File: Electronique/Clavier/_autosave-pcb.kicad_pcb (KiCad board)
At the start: 2 copper layers, 170 parts, among them J3 Conn_01x05, Q3 BSS84, Q4 BSS138, SW1 A, SW10 R, SW11 F, SW12 C, SW13 T, SW14 G, SW15 V, SW16 Y, SW17 H, SW18 B, SW19 1, SW2 Q, SW20 2, SW21 3, SW22 4, SW23 5, SW24 6, SW25 7, SW26 U, SW27 J, SW28 N, SW29 8, SW3 <, SW30 I, SW31 K, SW32 ,, SW33 9, SW34 O, SW35 L, SW36 ;, SW37 0, SW38 P, SW39 M, SW4 Z, SW40 :, SW41 SW_Push, SW42 SW_Push, SW43 ², SW44 Tab, SW45 VMaj, SW46 Shift, SW47 Echap, SW48 F1, SW49 F2, SW5 S, SW50 F3, SW51 F4, SW52 F5, SW53 F6, SW54 F7, SW55 F8, SW56 F9, SW57 F10, SW58 F11, SW59 ), SW6 W, SW60 ^, SW61 ù, SW62 !, SW63 F12, SW64 =, SW65 $, SW66 *, SW67 Up, SW7 E, SW8 D, SW9 X, U1 ESP32-S3-WROOM-1, U3 USBLC6-2P6, U4 TLV75533PDBV, U6 MCP73871-2CC

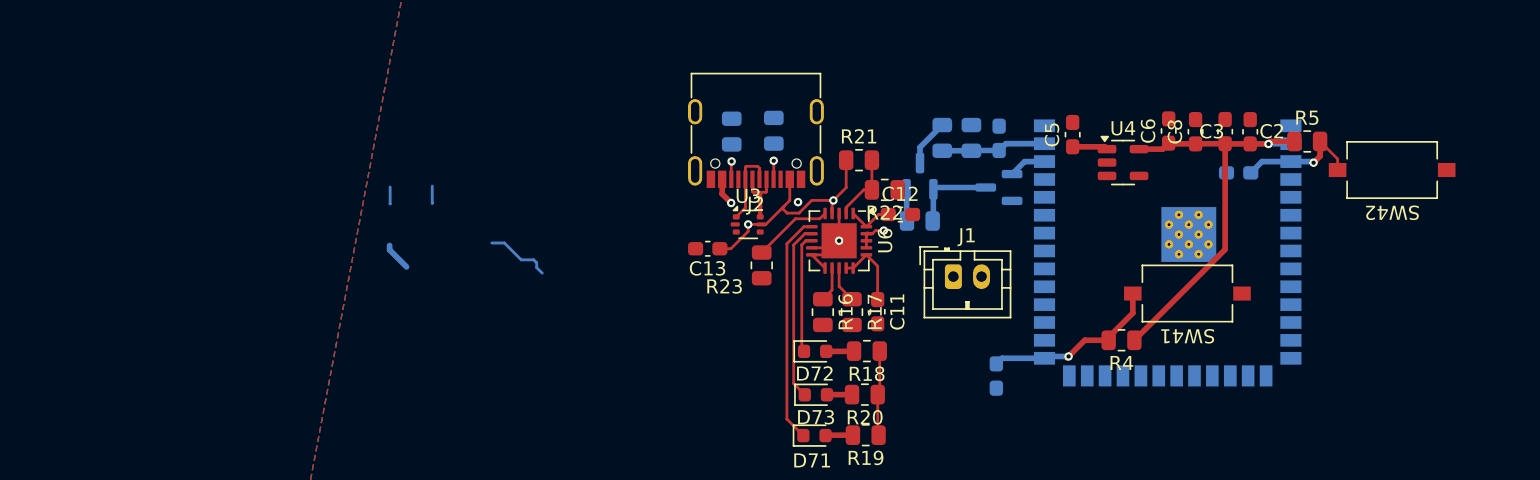
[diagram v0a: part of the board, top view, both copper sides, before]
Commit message: update keyboard schematic
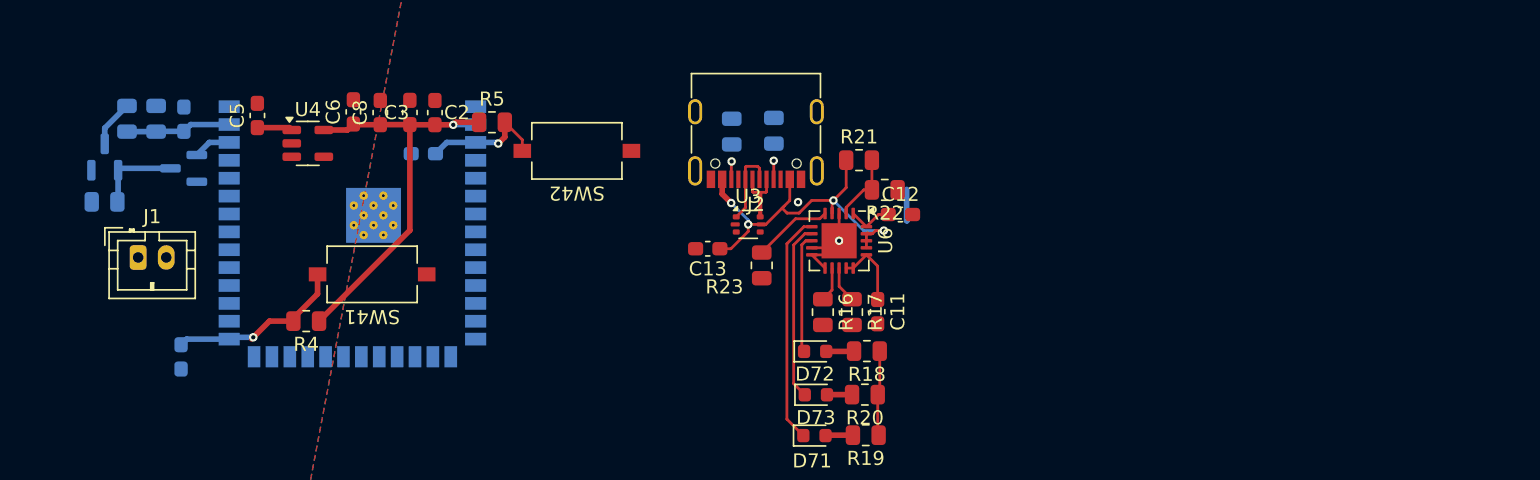
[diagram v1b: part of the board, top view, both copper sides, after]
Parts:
- moved SW41 57.9 mm to (305.4, -115.2)
- moved C1 57.9 mm to (291.8, -109.3)
- moved C3 57.9 mm to (308.1, -126.7)
- moved C4 57.9 mm to (292.0, -126.2)
- moved C6 57.9 mm to (304.1, -126.7)
- moved J1 57.9 mm to (288.8, -116.4)
- moved Q4 57.9 mm to (292.0, -122.7)
- moved R9 57.9 mm to (286.4, -120.3)
- moved U4 57.9 mm to (300.8, -124.5)
- moved C2 57.9 mm to (309.9, -126.7)
- moved C5 57.9 mm to (297.2, -126.5)
- moved C7 57.9 mm to (309.0, -123.8)
- moved C8 57.9 mm to (306.0, -126.7)
- moved Q3 57.9 mm to (286.4, -123.5)
- moved R4 57.9 mm to (300.7, -111.9)
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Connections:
- J2 pad S1: unconnected-(J2-SHIELD-PadS1)_2 -> GND
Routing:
- net Net-(J2-CC1): track 2.55 -> 1.32 mm
- net Net-(J2-CC2): track 2.49 -> 1.28 mm
